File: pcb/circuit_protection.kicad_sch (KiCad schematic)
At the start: 17 parts

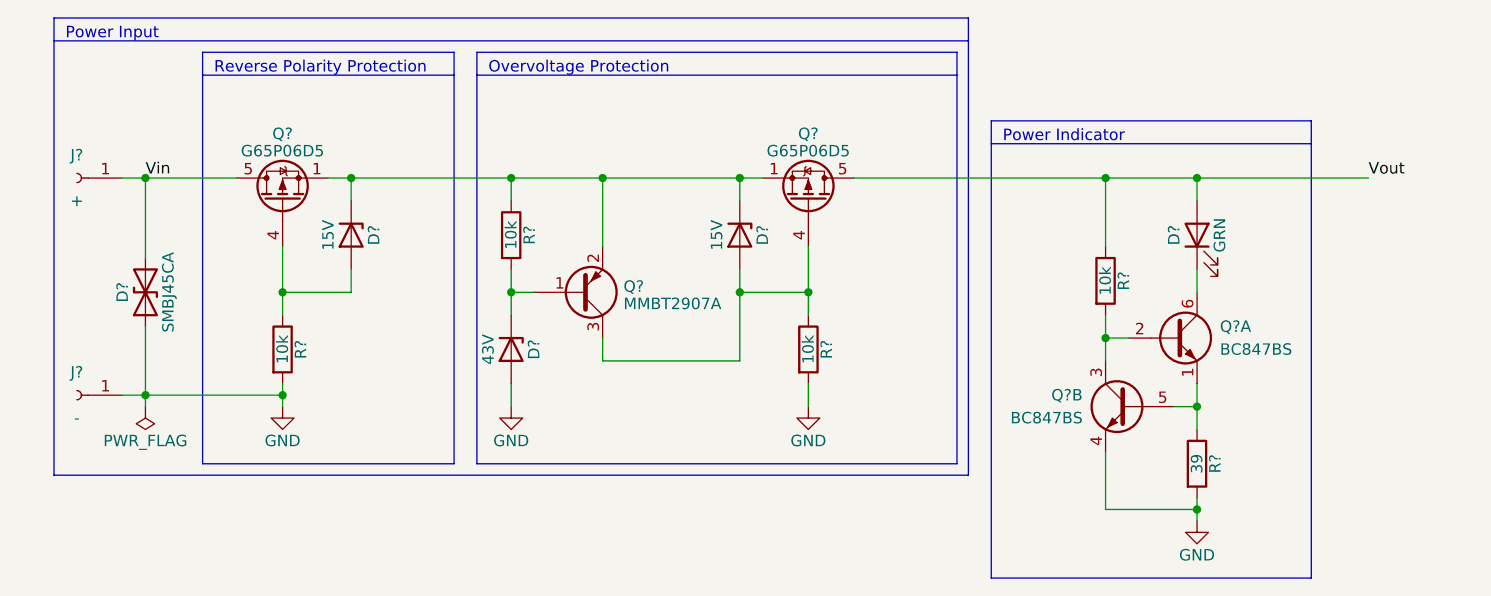
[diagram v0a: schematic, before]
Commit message: set Vin/Vout footprint
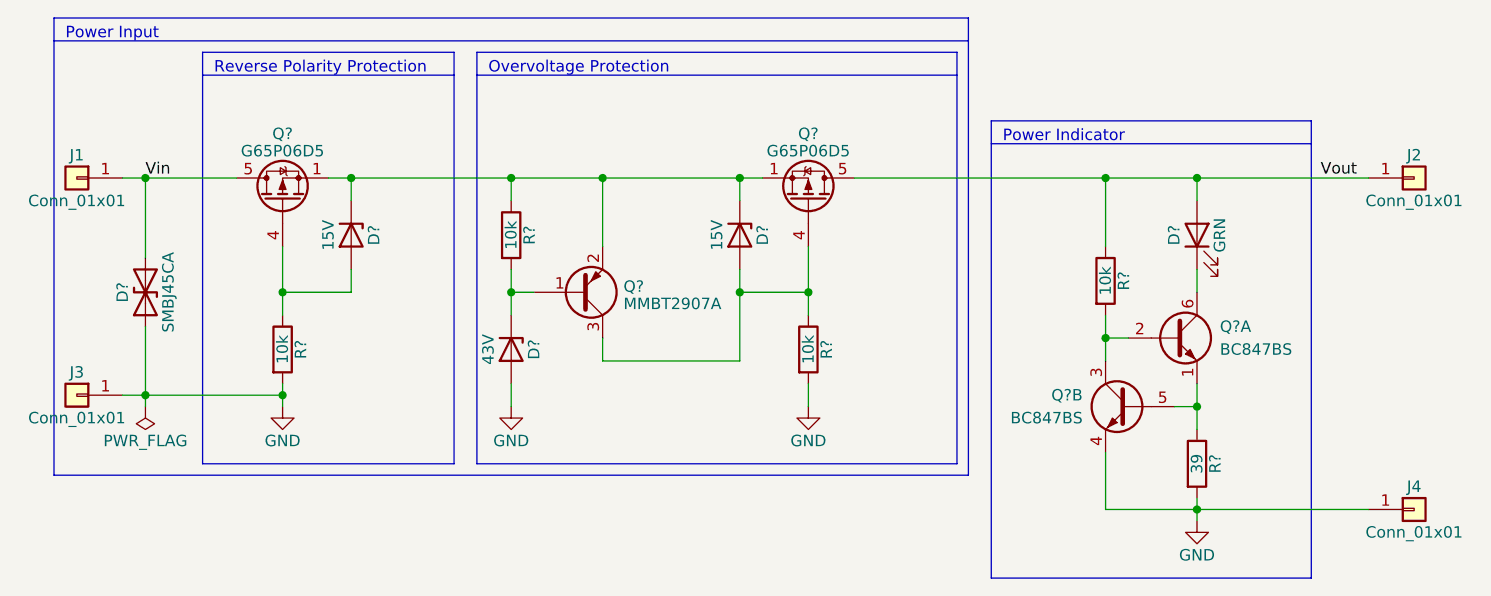
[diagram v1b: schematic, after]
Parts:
- removed J?: -, pl_banana:CT3151SP, symbol Connector:Conn_01x01_Socket
- removed J?: +, pl_banana:CT3151SP, symbol Connector:Conn_01x01_Socket
- added J1, J2, J3, J4: Conn_01x01, Connector_Wire:SolderWirePad_1x01_SMD_5x10mm, symbol Connector_Generic:Conn_01x01
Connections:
- net GND: now also J3.1 (Pin_1), J4.1 (Pin_1)
- net Vin: now also J1.1 (Pin_1)
- net Vout: now also J2.1 (Pin_1)
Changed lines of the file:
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@@
+    (stroke (width 0) (type default))
+  )
+  (wire (pts (xy 209.55 111.76) (xy 228.6 111.76))
     (stroke (width 0) (type default))
   )
@@
     (effects (font (size 1.27 1.27)) (justify left bottom))
   )
-  (label "Vout" (at 228.6 74.93 0) (fields_autoplaced)
-    (effects (font (size 1.27 1.27)) (justify left bottom))
-  )
-  (symbol (lib_id "Connector:Conn_01x01_Socket") (at 85.09 99.06 0) (mirror y) (unit 1)
-    (in_bom yes) (on_board yes) (dnp no)
-    (property "Reference" "J?" (at 85.09 96.52 0)
-      (effects (font (size 1.27 1.27)))
-    )
-    (property "Value" "-" (at 85.09 101.6 0)
-      (effects (font (size 1.27 1.27)))
-    )
-    (property "Footprint" "pl_banana:CT3151SP" (at 85.09 99.06 0)
-      (effects (font (size 1.27 1.27)) hide)
-    )
-    (property "Datasheet" "~" (at 85.09 99.06 0)
-      (effects (font (size 1.27 1.27)) hide)
-    )
-    (property "MPN" "CT3151SP-0" (at 85.09 99.06 0)
-      (effects (font (size 1.27 1.27)) hide)
-    )
-    (property "Manufacture" "Cal Test" (at 85.09 99.06 0)
-      (effects (font (size 1.27 1.27)) hide)
-    )
-    (property "Power" "~" (at 85.09 99.06 0)
-      (effects (font (size 1.27 1.27)) hide)
-    )
-    (property "SPN" "BKCT3151SP-0-ND" (at 85.09 99.06 0)
-      (effects (font (size 1.27 1.27)) hide)
-    )
-    (property "Supplier" "Digi-Key" (at 85.09 99.06 0)
-      (effects (font (size 1.27 1.27)) hide)
-    )
-    (property "Tolerance" "~" (at 85.09 99.06 0)
-      (effects (font (size 1.27 1.27)) hide)
-    )
-    (property "Voltage" "~" (at 85.09 99.06 0)
-      (effects (font (size 1.27 1.27)) hide)
-    )
-    (pin "1")
-    (instances
-      (project "pbh"
-        (path "/7400425b-2b7e-4dc1-bb4a-4409b0a7483f"
-          (reference "J?") (unit 1)
-        )
-        (path "/7400425b-2b7e-4dc1-bb4a-4409b0a7483f/cf7d8134-9a31-4bbc-82eb-57482d3e4b91"
-          (reference "J4") (unit 1)
-        )
-      )
-      (project "pbh_power"
-        (path "/ca7b1b2c-b03d-4924-8368-3b490fd3021c"
-          (reference "J?") (unit 1)
-        )
-      )
-      (project "circuit_protection"
-        (path "/f599416d-cdc4-40c7-ae75-1821ef9484d3"
-          (reference "J2") (unit 1)
-        )
-      )
-    )
+  (label "Vout" (at 227.33 74.93 180) (fields_autoplaced)
+    (effects (font (size 1.27 1.27)) (justify right bottom))
   )
   (symbol (lib_id "pl_MOSFET:G65P06D5") (at 107.95 74.93 90) (unit 1)
@@
         (path "/f599416d-cdc4-40c7-ae75-1821ef9484d3"
           (reference "Q1") (unit 1)
+        )
+      )
+    )
+  )
+  (symbol (lib_id "Connector_Generic:Conn_01x01") (at 233.68 74.93 0) (unit 1)
+    (in_bom yes) (on_board yes) (dnp no)
+    (property "Reference" "J2" (at 233.68 72.39 0)
+      (effects (font (size 1.27 1.27)))
+    )
+    (property "Value" "Conn_01x01" (at 233.68 77.47 0)
+      (effects (font (size 1.27 1.27)))
+    )
+    (property "Footprint" "Connector_Wire:SolderWirePad_1x01_SMD_5x10mm" (at 233.68 74.93 0)
+      (effects (font (size 1.27 1.27)) hide)
+    )
+    (property "Datasheet" "~" (at 233.68 74.93 0)
+      (effects (font (size 1.27 1.27)) hide)
+    )
+    (pin "1")
+    (instances
+      (project "circuit_protection"
+        (path "/f599416d-cdc4-40c7-ae75-1821ef9484d3"
+          (reference "J2") (unit 1)
         )
       )
@@
     )
   )
-  (symbol (lib_id "Connector:Conn_01x01_Socket") (at 85.09 74.93 0) (mirror y) (unit 1)
-    (in_bom yes) (on_board yes) (dnp no)
-    (property "Reference" "J?" (at 85.09 72.39 0)
-      (effects (font (size 1.27 1.27)))
-    )
-    (property "Value" "+" (at 85.09 77.47 0)
-      (effects (font (size 1.27 1.27)))
-    )
-    (property "Footprint" "pl_banana:CT3151SP" (at 85.09 74.93 0)
-      (effects (font (size 1.27 1.27)) hide)
-    )
-    (property "Datasheet" "~" (at 85.09 74.93 0)
-      (effects (font (size 1.27 1.27)) hide)
-    )
-    (property "MPN" "CT3151SP-2" (at 85.09 74.93 0)
-      (effects (font (size 1.27 1.27)) hide)
-    )
-    (property "Manufacture" "Cal Test" (at 85.09 74.93 0)
-      (effects (font (size 1.27 1.27)) hide)
-    )
-    (property "Power" "~" (at 85.09 74.93 0)
-      (effects (font (size 1.27 1.27)) hide)
-    )
-    (property "SPN" "BKCT3151SP-2-ND" (at 85.09 74.93 0)
-      (effects (font (size 1.27 1.27)) hide)
-    )
-    (property "Supplier" "Digi-Key" (at 85.09 74.93 0)
-      (effects (font (size 1.27 1.27)) hide)
-    )
-    (property "Tolerance" "~" (at 85.09 74.93 0)
-      (effects (font (size 1.27 1.27)) hide)
-    )
-    (property "Voltage" "~" (at 85.09 74.93 0)
-      (effects (font (size 1.27 1.27)) hide)
-    )
-    (pin "1")
-    (instances
-      (project "pbh"
-        (path "/7400425b-2b7e-4dc1-bb4a-4409b0a7483f"
-          (reference "J?") (unit 1)
-        )
-        (path "/7400425b-2b7e-4dc1-bb4a-4409b0a7483f/cf7d8134-9a31-4bbc-82eb-57482d3e4b91"
-          (reference "J3") (unit 1)
-        )
-      )
-      (project "pbh_power"
-        (path "/ca7b1b2c-b03d-4924-8368-3b490fd3021c"
-          (reference "J?") (unit 1)
-        )
-      )
-      (project "circuit_protection"
-        (path "/f599416d-cdc4-40c7-ae75-1821ef9484d3"
-          (reference "J1") (unit 1)
-        )
-      )
-    )
-  )
   (symbol (lib_id "power:PWR_FLAG") (at 92.71 100.33 180) (unit 1)
     (in_bom yes) (on_board yes) (dnp no)
@@
         )
       )
+    )
+  )
+  (symbol (lib_id "Connector_Generic:Conn_01x01") (at 233.68 111.76 0) (unit 1)
+    (in_bom yes) (on_board yes) (dnp no)
+    (property "Reference" "J4" (at 233.68 109.22 0)
+      (effects (font (size 1.27 1.27)))
+    )
+    (property "Value" "Conn_01x01" (at 233.68 114.3 0)
+      (effects (font (size 1.27 1.27)))
+    )
+    (property "Footprint" "Connector_Wire:SolderWirePad_1x01_SMD_5x10mm" (at 233.68 111.76 0)
+      (effects (font (size 1.27 1.27)) hide)
+    )
+    (property "Datasheet" "~" (at 233.68 111.76 0)
+      (effects (font (size 1.27 1.27)) hide)
+    )
+    (pin "1")
+    (instances
+      (project "circuit_protection"
+        (path "/f599416d-cdc4-40c7-ae75-1821ef9484d3"
+          (reference "J4") (unit 1)
+        )
+      )
+    )
+  )
+  (symbol (lib_id "Connector_Generic:Conn_01x01") (at 85.09 74.93 0) (mirror y) (unit 1)
+    (in_bom yes) (on_board yes) (dnp no)
+    (property "Reference" "J1" (at 85.09 72.39 0)
+      (effects (font (size 1.27 1.27)))
+    )
+    (property "Value" "Conn_01x01" (at 85.09 77.47 0)
+      (effects (font (size 1.27 1.27)))
+    )
+    (property "Footprint" "Connector_Wire:SolderWirePad_1x01_SMD_5x10mm" (at 85.09 74.93 0)
+      (effects (font (size 1.27 1.27)) hide)
+    )
+    (property "Datasheet" "~" (at 85.09 74.93 0)
+      (effects (font (size 1.27 1.27)) hide)
+    )
+    (pin "1")
+    (instances
+      (project "circuit_protection"
+        (path "/f599416d-cdc4-40c7-ae75-1821ef9484d3"
+          (reference "J1") (unit 1)
+        )
+      )
+    )
+  )
+  (symbol (lib_id "Connector_Generic:Conn_01x01") (at 85.09 99.06 0) (mirror y) (unit 1)
+    (in_bom yes) (on_board yes) (dnp no)
+    (property "Reference" "J3" (at 85.09 96.52 0)
+      (effects (font (size 1.27 1.27)))
+    )
+    (property "Value" "Conn_01x01" (at 85.09 101.6 0)
+      (effects (font (size 1.27 1.27)))
+    )
+    (property "Footprint" "Connector_Wire:SolderWirePad_1x01_SMD_5x10mm" (at 85.09 99.06 0)
+      (effects (font (size 1.27 1.27)) hide)
+    )
+    (property "Datasheet" "~" (at 85.09 99.06 0)
+      (effects (font (size 1.27 1.27)) hide)
+    )
+    (pin "1")
+    (instances
+      (project "circuit_protection"
+        (path "/f599416d-cdc4-40c7-ae75-1821ef9484d3"
+          (reference "J3") (unit 1)
+        )
+      )

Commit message: remove LED
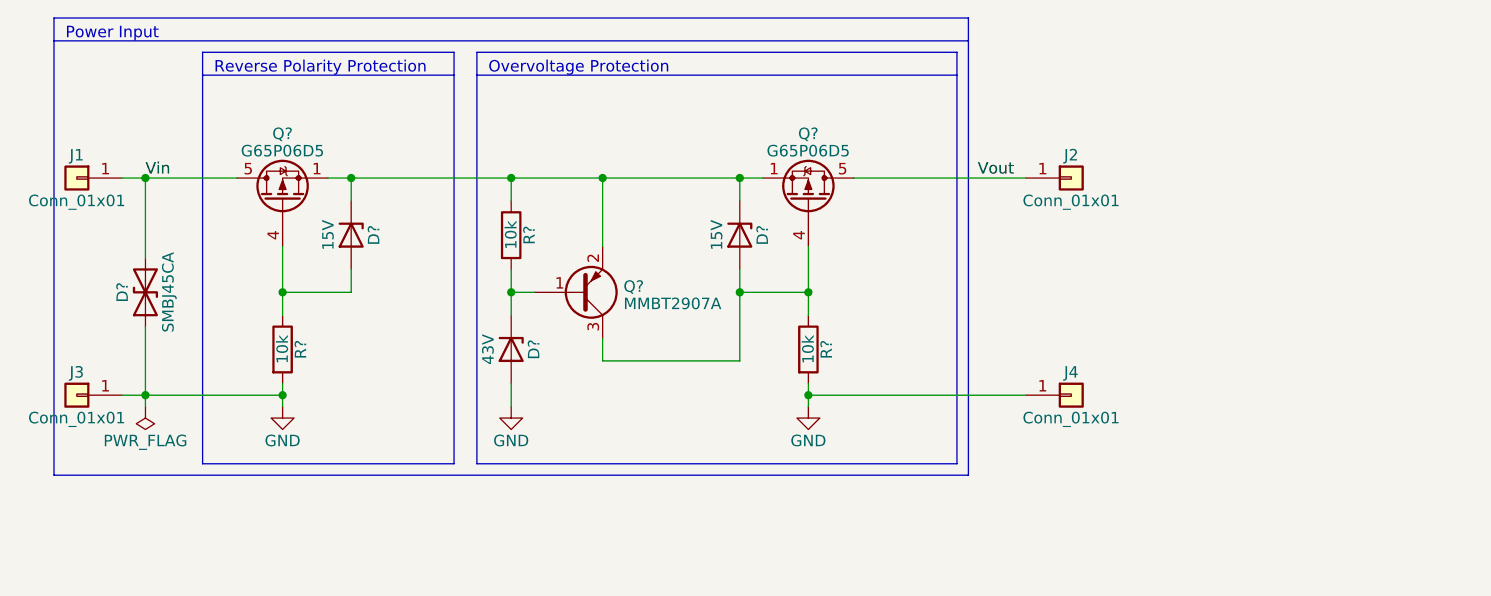
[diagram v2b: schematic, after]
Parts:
- removed D?: GRN, LED_SMD:LED_PLCC-2_3.4x3.0mm_KA, symbol Device:LED
- removed Q? (x2): BC847BS, Package_TO_SOT_SMD:SOT-363_SC-70-6, symbol Transistor_BJT:BC847BS
- removed R?: 10k, Resistor_SMD:R_0603_1608Metric, symbol Device:R
- removed R?: 39, Resistor_SMD:R_0603_1608Metric, symbol Device:R
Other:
- note removed: "Power Indicator"
- moved on the sheet: J2, J4
